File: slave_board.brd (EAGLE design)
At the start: 198.8 x 99.4 mm, 155 parts, among them IC3 ATMEGA2560-16AU, J11 1935161, J17 RJ45, J22 RJ45, J3 1935161, J6 1935161, K1 ORWH-SH-112D1F, Q1 PHB45NQ15T, Q2 PHB45NQ15T, Q3 BSS138L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

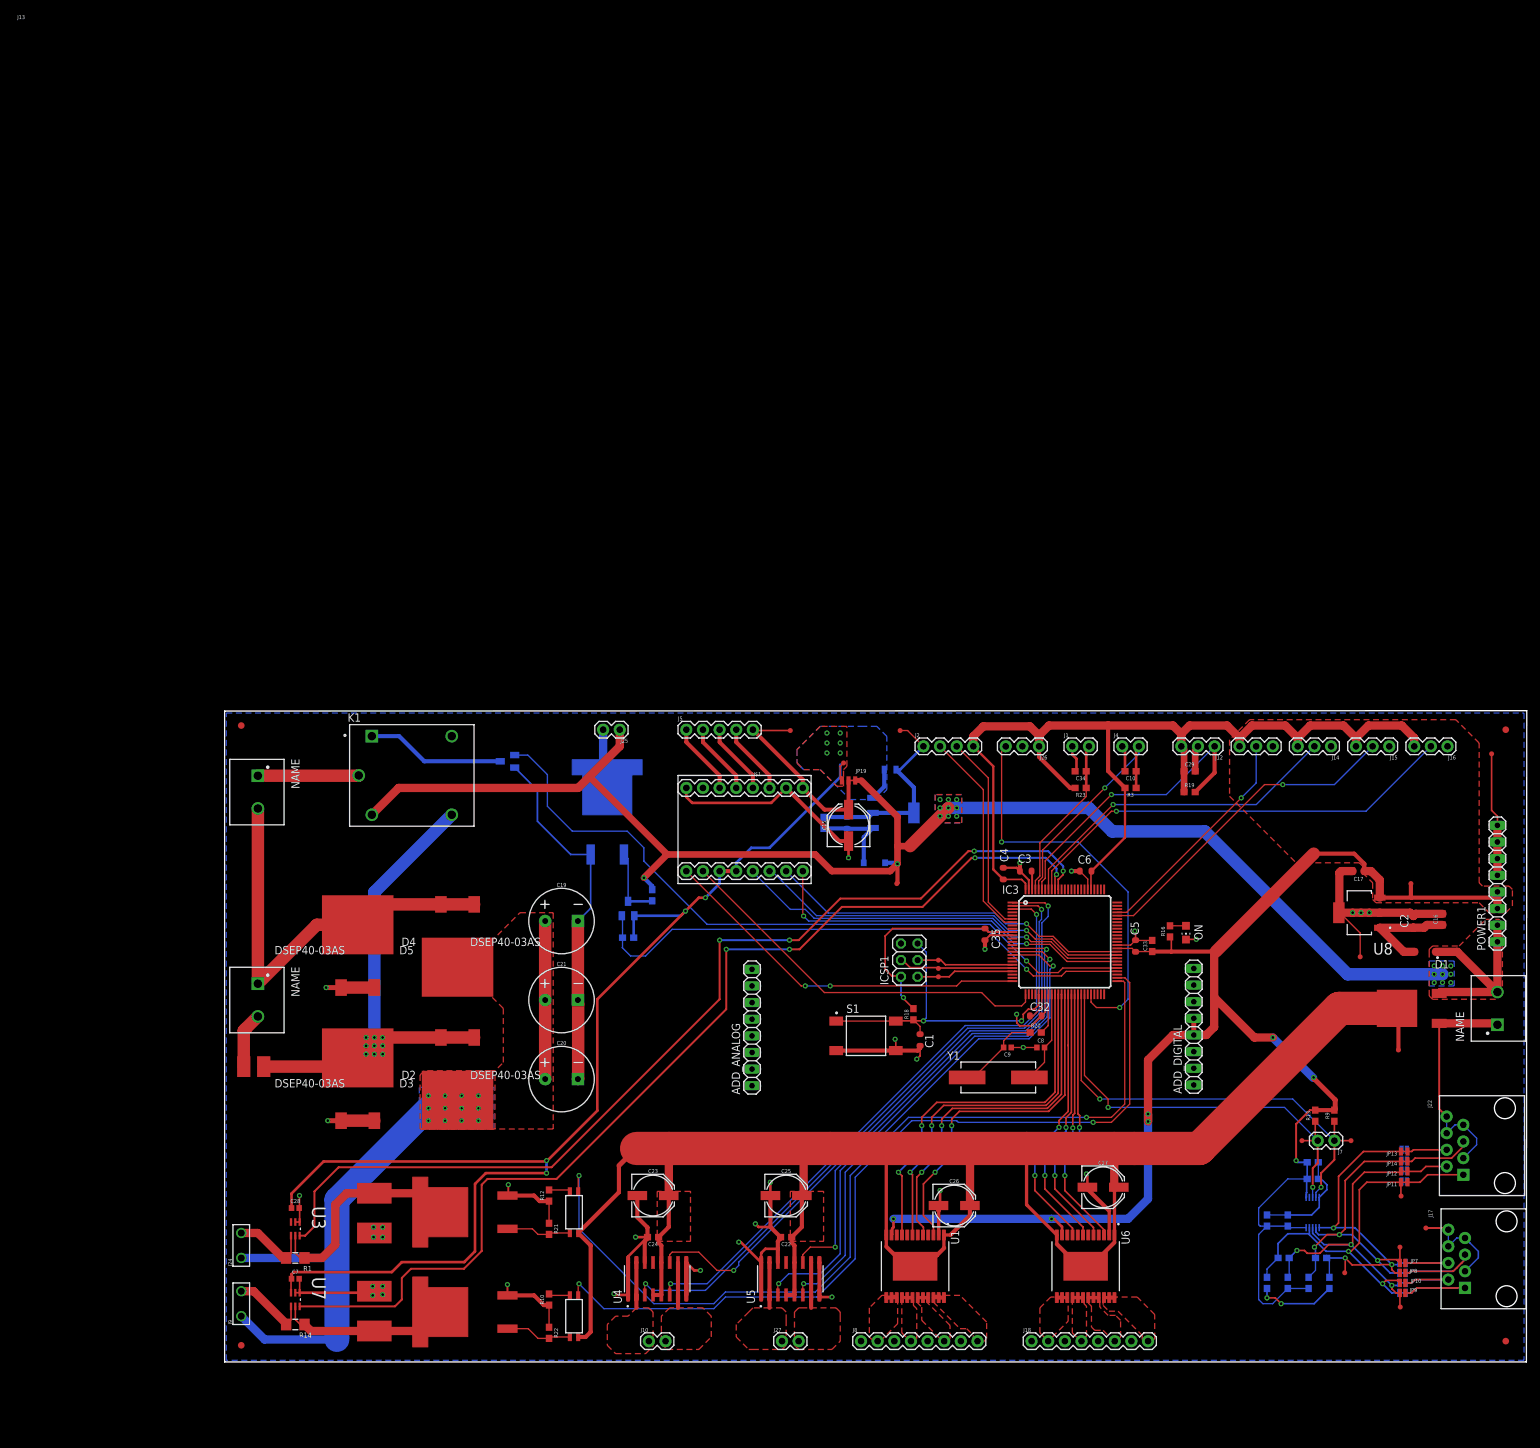
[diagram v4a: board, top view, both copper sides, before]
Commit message: board progress - routing additional digital plus analog
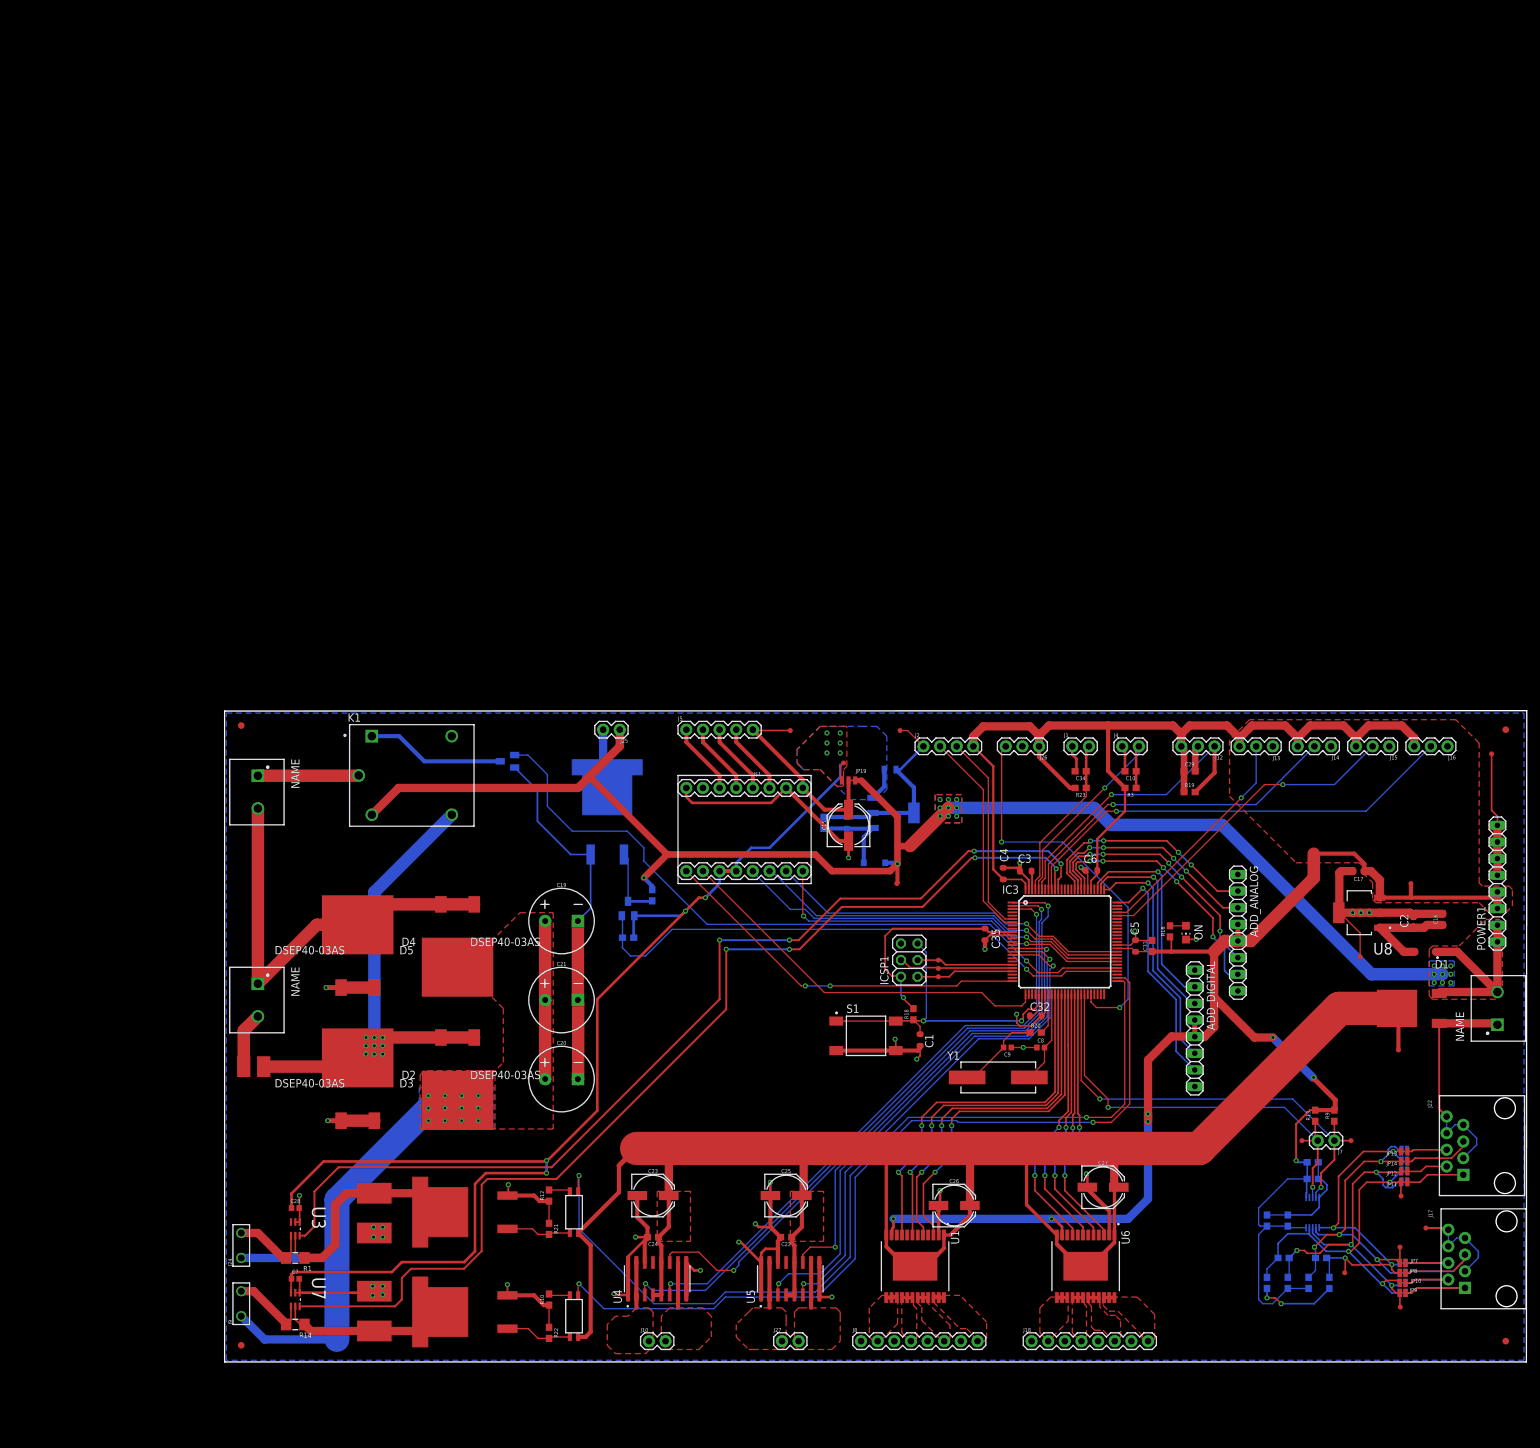
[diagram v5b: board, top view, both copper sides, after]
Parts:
- moved ADD_ANALOG 75.6 mm to (154.7, 65.5), turned to 270 degrees
- moved C6 0.89 mm to (132.3, 75.0)
- moved ADD_DIGITAL 0.30 mm to (148.1, 50.9), turned to 270 degrees
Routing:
- net ADD_A15: track 0.00 -> 40.1 mm, vias 0 -> 5
- net ADD_A14: track 0.00 -> 39.1 mm, vias 0 -> 5
- net ADD_D24: track 0.00 -> 36.1 mm, vias 0 -> 1
- net ADD_D25: track 0.00 -> 35.8 mm, vias 0 -> 1
- net ADD_A12: track 0.00 -> 35.5 mm, vias 0 -> 4
- net ADD_A13: track 0.00 -> 35.1 mm, vias 0 -> 4
- net ADD_D22: track 0.00 -> 31.7 mm, vias 0 -> 1
- net ADD_D23: track 0.00 -> 31.5 mm, vias 0 -> 1
- net V-12V_PROT: track 304.6 -> 321.1 mm
- net DSDA+: track 53.8 -> 59.5 mm, vias 3 -> 4
- net +5V: track 452.8 -> 457.8 mm
- net DSCL+: track 50.2 -> 54.9 mm, vias 3 -> 4
- net DSDA-: track 52.4 -> 54.9 mm, vias 2 -> 3
- net DSCL-: track 52.4 -> 54.4 mm, vias 3 -> 4
- net ELEV_ENC_OUT: track 61.4 -> 60.1 mm
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
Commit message: board progress
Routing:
- net V-HVDC: track 95.9 -> 98.1 mm
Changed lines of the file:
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@@
 <wire x1="17.145" y1="3.429" x2="17.145" y2="24.765" width="3.81" layer="16"/>
 <wire x1="17.145" y1="24.765" x2="31.115" y2="38.735" width="3.81" layer="16"/>
+<wire x1="35.56" y1="39.9415" x2="34.8615" y2="40.64" width="1.27" layer="1"/>
+<wire x1="34.8615" y1="40.64" x2="33.655" y2="40.64" width="1.27" layer="1"/>
 <wire x1="17.145" y1="24.765" x2="17.145" y2="15.875" width="0" layer="19" extent="16-16"/>
 </signal>

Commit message: Fixed some errors
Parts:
- added C36, C37: 0.1uF, rcl:C0603
- added TP1, TP20: TEST-POINT3, SparkFun-Connectors:PAD.03X.03
- C1, C3, C32, C35, C4, C6: device SmartPrj:C0603-ROUND -> rcl:C0603
- C11, C12, C13, C14, C22, C24, C33: device SparkFun-Capacitors:0603 -> rcl:C0603
- C28, C7, C8, C9: device SparkFun-Capacitors:0402 -> rcl:C0603
- C5: value 100n -> 100nF; device SmartPrj:C0603-ROUND -> rcl:C0603
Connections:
- net CURR_SENS0: now also C36.1, TP1.P$1
- net CURR_SENS1: now also C37.1, TP20.P$1
- net GND: now also C36.2, C37.2
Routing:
- net GND: track 476.1 -> 467.0 mm, vias 37 -> 36
- net CURR_SENS1: track 153.7 -> 157.9 mm
- net CURR_SENS0: track 160.9 -> 163.6 mm

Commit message: Fixed some errors
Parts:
- moved TP1 117.4 mm to (112.6, 75.2)
- moved TP20 109.2 mm to (112.4, 77.1)
